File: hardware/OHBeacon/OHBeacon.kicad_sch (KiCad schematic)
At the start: 10 parts, among them J1 Conn_01x04_Socket, SW1 SW_Push, U1 ESP32-C3-WROOM-02

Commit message: new sch
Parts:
- added C1, C10, C11, C12, C13, C14, C2, C3, C4, C5, C6, C7, C8, C9: 0.1uF, Capacitor_SMD:C_0603_1608Metric, symbol Device:C
- added C18: 1.0uF, Capacitor_SMD:C_0603_1608Metric, symbol Device:C
- added C19, C20: 4.7uF, Capacitor_SMD:C_0603_1608Metric, symbol Device:C
- added D1, D10, D11, D12, D2, D3, D4, D5, D6, D7, D8, D9: WS2812B, LED_SMD:LED_WS2812B_PLCC4_5.0x5.0mm_P3.2mm, symbol LED:WS2812B
- added D14, D30: MDB6S, Package_SO:TSSOP-4_4.4x5mm_P4mm, symbol Diode_Bridge:MDB6S
- added J2, J3, J5, J6: Conn_01x01_Pin, Connector_Wire:SolderWire-2sqmm_1x01_D2mm_OD3.9mm, symbol Connector:Conn_01x01_Pin
- added J4: USB_C_Receptacle_PowerOnly_6P, Connector_USB:USB_C_Receptacle_GCT_USB4135-GF-A_6P_TopMnt_Horizontal, symbol Connector:USB_C_Receptacle_PowerOnly_6P
- added J7: Conn_01x02_Pin, Connector_PinSocket_2.54mm:PinSocket_1x02_P2.54mm_Vertical, symbol Connector:Conn_01x02_Pin
- added Q1: DMG2305UX-7, DMG2305UX-7:SOT91P240X110-3N_DMG2305UX-7, symbol DMG2305UX-7:DMG2305UX-7
- added R1, R5: 10k, Resistor_SMD:R_0603_1608Metric, symbol Device:R
- added R6, R7, R8: 100k, Resistor_SMD:R_0603_1608Metric, symbol Device:R
- added R9: 1k, Resistor_SMD:R_0603_1608Metric, symbol Device:R
- added SW2: SW_Push, Button_Switch_THT:SW_PUSH_6mm, symbol Switch:SW_Push
- added U2: BQ24074RGT, Package_DFN_QFN:VQFN-16-1EP_3x3mm_P0.5mm_EP1.6x1.6mm, symbol Battery_Management:BQ24074RGT
- added U3: AP2112K-3.3, Package_TO_SOT_SMD:SOT-23-5, symbol Regulator_Linear:AP2112K-3.3
- C17: value 0.1uF -> 4.7uF
- SW1: footprint Buttons_Switches_THT.pretty-master:SW_PUSH_6mm -> Button_Switch_THT:SW_PUSH_6mm
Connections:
- net +3.3V: now also C1.1, C10.1, C11.1, C12.1, C18.1, C2.1, C3.1, C4.1, C5.1, C6.1, C7.1, C8.1, C9.1, D1.1 (VDD), D10.1 (VDD), D11.1 (VDD), D12.1 (VDD), D2.1 (VDD), D3.1 (VDD), D4.1 (VDD), D5.1 (VDD), D6.1 (VDD), D7.1 (VDD), D8.1 (VDD), D9.1 (VDD), R1.1, U3.5 (VOUT)
- net GND: now also U1.19 (GND), U1.9 (GND), C1.2, C10.2, C11.2, C12.2, C13.2, C14.2, C18.2, C19.2, C2.2, C20.2, C3.2, C4.2, C5.2, C6.2, C7.2, C8.2, C9.2, D1.3 (VSS), D10.3 (VSS), D11.3 (VSS), D12.3 (VSS), D14.2 (-), D2.3 (VSS), D3.3 (VSS), D30.2 (-), D4.3 (VSS), D5.3 (VSS), D6.3 (VSS), D7.3 (VSS), D8.3 (VSS), D9.3 (VSS), J4.A12 (GND), J4.B12 (GND), J7.1 (Pin_1), R5.1, R7.1, R8.1, R9.1, SW2.1, U2.14 (TMR), U2.17 (VSS), U2.4 (~{CE}), U2.8 (VSS), U3.2 (GND)
- net EN: now reaches R3.2, SW1.2, U1.2 (EN)
- net EN: now also C13.1; no longer C17.1
- net DIN: now reaches U1.15 (IO3)
- net DIN: now also D1.4 (DIN)
- net IO9: now reaches U1.8 (IO9)
- net IO9: now also C14.1, R1.2, SW2.2
- new net: C20.1, U2.10 (OUT), U2.11 (OUT)
- new net: Q1.3, R8.2, U3.3 (EN)
- new net: R5.2, U2.1 (TS)
- new net: R9.2, U2.16 (ISET)
- new net: R7.2, U2.5 (EN2)
- new net: R6.2, U2.6 (EN1)
- new net: D30.3, J3.1 (Pin_1)
- new net: D30.4, J2.1 (Pin_1)
- new net: D10.2 (DOUT), D12.4 (DIN)
- new net: D5.2 (DOUT), D7.4 (DIN)
- new net: D3.2 (DOUT), D5.4 (DIN)
- new net: D1.2 (DOUT), D3.4 (DIN)
- new net: D4.2 (DOUT), D6.4 (DIN)
- new net: D2.2 (DOUT), D4.4 (DIN)
- new net: D11.4 (DIN), D9.2 (DOUT)
- new net: D7.2 (DOUT), D9.4 (DIN)
- new net: D10.4 (DIN), D8.2 (DOUT)
- new net: D6.2 (DOUT), D8.4 (DIN)
- new net: D14.3, J6.1 (Pin_1)
- new net: D14.4, J5.1 (Pin_1)
- new net +5V: C17.1, D14.1 (+), D30.1 (+), J4.A9 (VBUS), J4.B9 (VBUS), Q1.1, R6.1, U2.13 (IN)
- new net +BATT: C19.1, J7.2 (Pin_2), Q1.2, U2.2 (BAT), U2.3 (BAT), U3.1 (VIN)
- new net DCON: D11.2 (DOUT), D2.4 (DIN)
- no-connect marks 0 -> 18
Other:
- removed sheet LED_strip
- removed sheet power_input
- note added: "DRILL FOOTPRINT WITH 2MM DIAMETER WORKS FOR HAND SOLDER POGO PIN PART NUMBER: 0906-8-15-20-76-14-11-0"
- moved on the sheet: C15, C16, J1, R2, R4, U1

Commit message: prelim beacon pcb
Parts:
- added R10: 100k, Resistor_SMD:R_0603_1608Metric, symbol Device:R
- added R11: 0, Resistor_SMD:R_0603_1608Metric, symbol Device:R
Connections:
- net +5V: now also R10.2
- net GND: now also R10.1, R11.1
- net at U2.12 (ILIM): now also R11.2
- no-connect marks 18 -> 17
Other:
- moved on the sheet: R6, R7

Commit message: Changed some stuff in the schematic :)
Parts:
- added C21: 1.0uF, Capacitor_SMD:C_0603_1608Metric, symbol Device:C
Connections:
- net +BATT: now also C21.1
- net GND: now also C21.2
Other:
- moved on the sheet: C17

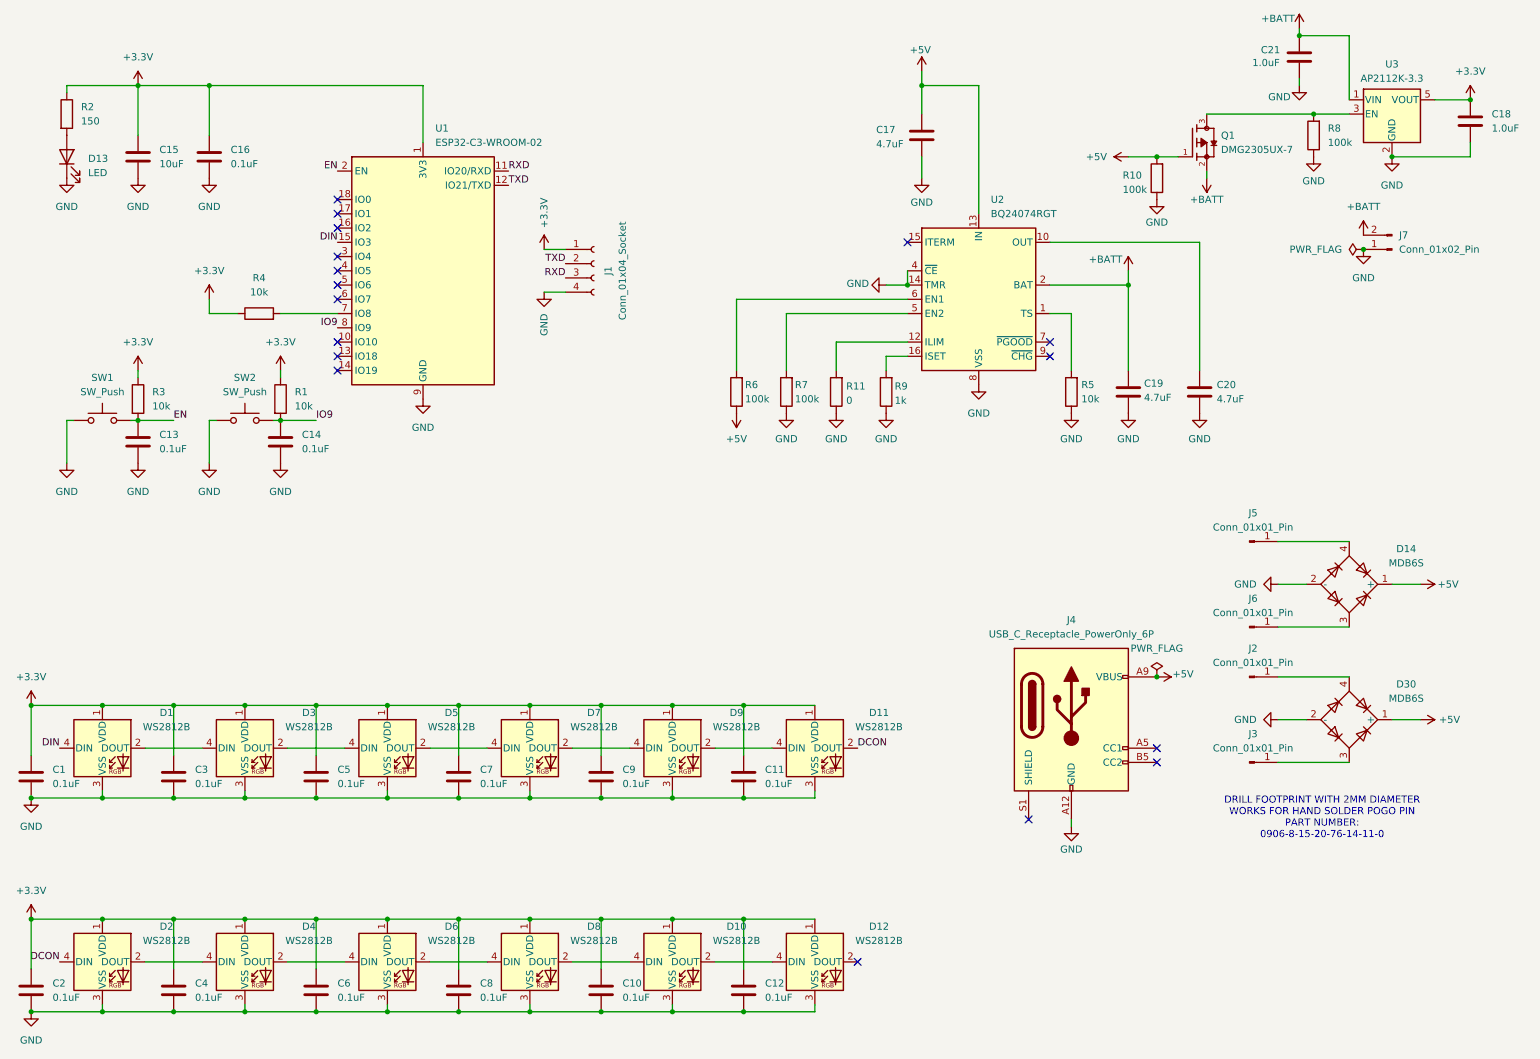
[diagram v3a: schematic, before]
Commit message: new oh beacon schematic and early routing
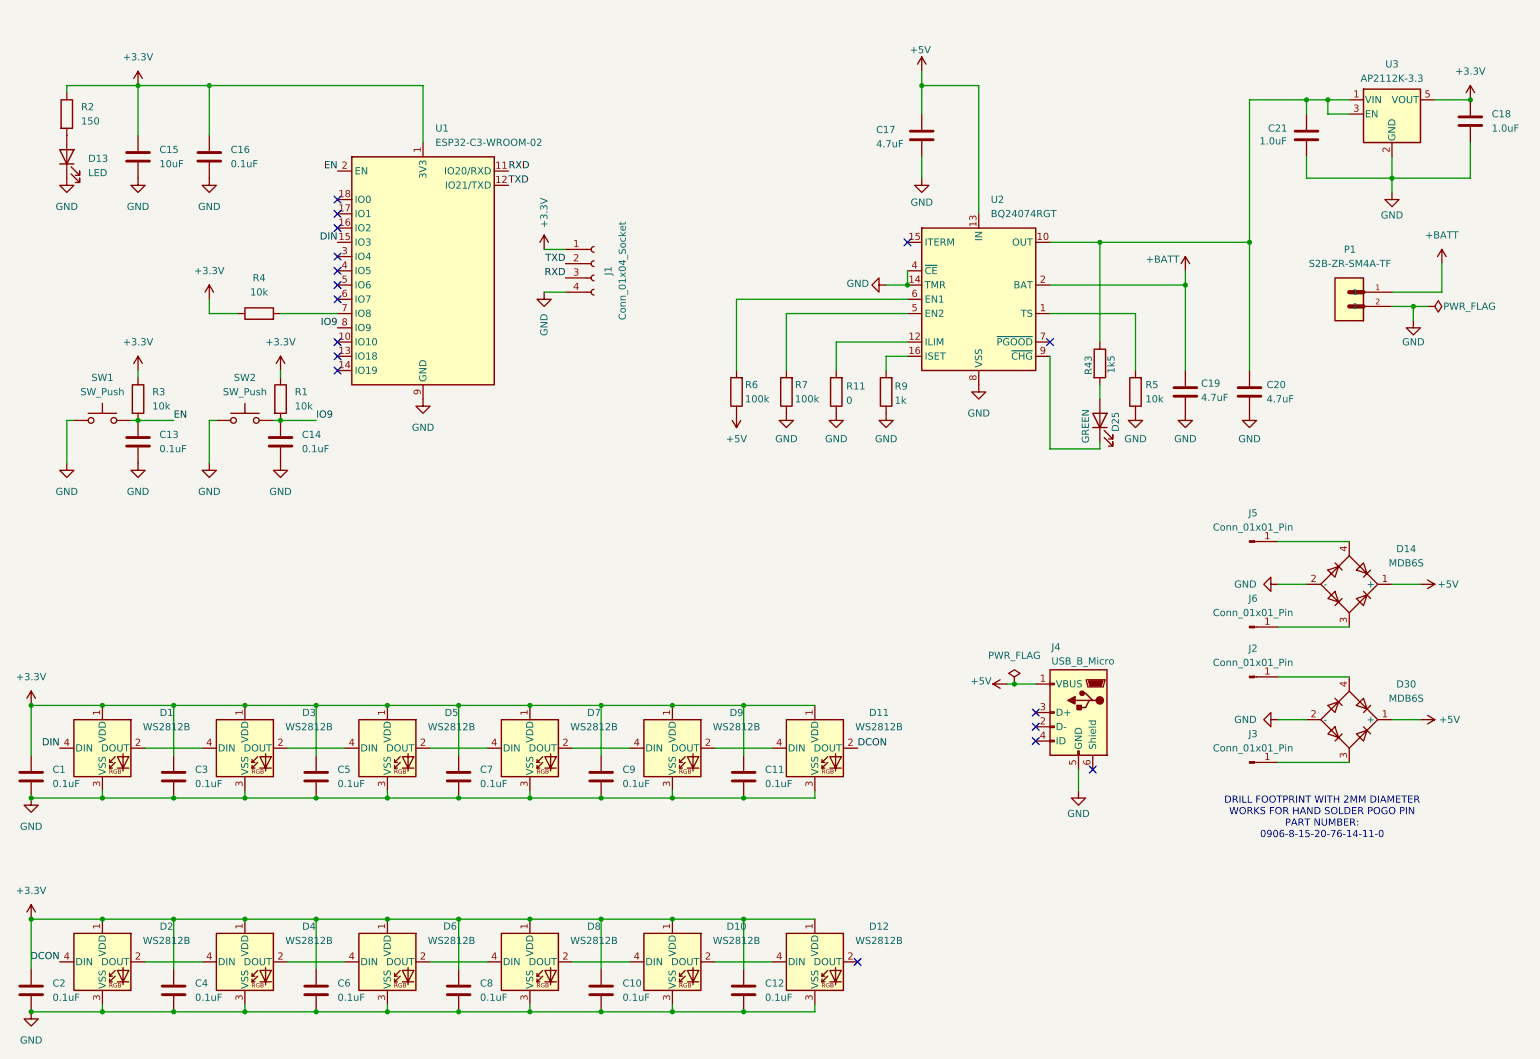
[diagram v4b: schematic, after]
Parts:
- removed J4: USB_C_Receptacle_PowerOnly_6P, Connector_USB:USB_C_Receptacle_GCT_USB4135-GF-A_6P_TopMnt_Horizontal, symbol Connector:USB_C_Receptacle_PowerOnly_6P
- removed J7: Conn_01x02_Pin, Connector_PinSocket_2.54mm:PinSocket_1x02_P2.54mm_Vertical, symbol Connector:Conn_01x02_Pin
- removed Q1: DMG2305UX-7, DMG2305UX-7:SOT91P240X110-3N_DMG2305UX-7, symbol DMG2305UX-7:DMG2305UX-7
- removed R10, R8: 100k, Resistor_SMD:R_0603_1608Metric, symbol Device:R
- added D25: GREEN, LED_SMD:LED_0603_1608Metric, symbol Device:LED
- added J4: USB_B_Micro, Connector_USB:USB_Micro-B_Wuerth_629105150521, symbol Connector:USB_B_Micro
- added P1: S2B-ZR-SM4A-TF, custom footprints:JST_S2B-ZR-SM4A-TF, symbol JST CONNECTOR:S2B-ZR-SM4A-TF
- added R43: 1k5, Resistor_SMD:R_0402_1005Metric, symbol Device:R
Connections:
- net +5V: now also J4.1 (VBUS)
- net +BATT: now also P1.1; no longer C21.1, U3.1 (VIN)
- net GND: now also J4.5 (GND), P1.2
- net at C20.1, U2.10 (OUT), U2.11 (OUT): now also C21.1, U3.1 (VIN), U3.3 (EN), R43.1
- net at U2.9 (~{CHG}): now also D25.1 (K)
- new net: D25.2 (A), R43.2
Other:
- moved on the sheet: C19, C20, C21, R5

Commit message: fml
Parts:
- removed C10, C11, C12, C9: 0.1uF, Capacitor_SMD:C_0603_1608Metric, symbol Device:C
- removed D10, D7, D8, D9: WS2812B, LED_SMD:LED_WS2812B_PLCC4_5.0x5.0mm_P3.2mm, symbol LED:WS2812B
- removed D14, D30: MDB6S, Package_SO:TSSOP-4_4.4x5mm_P4mm, symbol Diode_Bridge:MDB6S
- C1, C2, C3, C4, C5, C6, C7, C8: footprint Capacitor_SMD:C_0603_1608Metric -> Capacitor_SMD:C_0805_2012Metric_Pad1.18x1.45mm_HandSolder
- C10: renamed from C16; footprint Capacitor_SMD:C_0603_1608Metric -> Capacitor_SMD:C_0805_2012Metric_Pad1.18x1.45mm_HandSolder
- C11: renamed from C13; footprint Capacitor_SMD:C_0603_1608Metric -> Capacitor_SMD:C_0805_2012Metric_Pad1.18x1.45mm_HandSolder
- C12: renamed from C14; footprint Capacitor_SMD:C_0603_1608Metric -> Capacitor_SMD:C_0805_2012Metric_Pad1.18x1.45mm_HandSolder
- C13: renamed from C19; footprint Capacitor_SMD:C_0603_1608Metric -> Capacitor_SMD:C_0805_2012Metric_Pad1.18x1.45mm_HandSolder
- C14: renamed from C20; footprint Capacitor_SMD:C_0603_1608Metric -> Capacitor_SMD:C_0805_2012Metric_Pad1.18x1.45mm_HandSolder
- C15: renamed from C17; footprint Capacitor_SMD:C_0603_1608Metric -> Capacitor_SMD:C_0805_2012Metric_Pad1.18x1.45mm_HandSolder
- C16: renamed from C21; footprint Capacitor_SMD:C_0603_1608Metric -> Capacitor_SMD:C_0805_2012Metric_Pad1.18x1.45mm_HandSolder
- C17: renamed from C18; footprint Capacitor_SMD:C_0603_1608Metric -> Capacitor_SMD:C_0805_2012Metric_Pad1.18x1.45mm_HandSolder
- C9: renamed from C15; footprint Capacitor_SMD:C_0603_1608Metric -> Capacitor_SMD:C_0805_2012Metric_Pad1.18x1.45mm_HandSolder
- D10: renamed from D25; footprint LED_SMD:LED_0603_1608Metric -> LED_SMD:LED_0805_2012Metric_Pad1.15x1.40mm_HandSolder
- D9: renamed from D13; value LED -> RED; footprint LED_SMD:LED_0603_1608Metric -> LED_SMD:LED_0805_2012Metric_Pad1.15x1.40mm_HandSolder
- J1: renamed from J5; footprint Connector_Wire:SolderWire-2sqmm_1x01_D2mm_OD3.9mm -> Connector_Wire:SolderWire-1sqmm_1x01_D1.4mm_OD3.9mm
- J2: renamed from J6; footprint Connector_Wire:SolderWire-2sqmm_1x01_D2mm_OD3.9mm -> Connector_Wire:SolderWire-1sqmm_1x01_D1.4mm_OD3.9mm
- J3: renamed from J2; footprint Connector_Wire:SolderWire-2sqmm_1x01_D2mm_OD3.9mm -> Connector_Wire:SolderWire-1sqmm_1x01_D1.4mm_OD3.9mm
- J4: renamed from J3; footprint Connector_Wire:SolderWire-2sqmm_1x01_D2mm_OD3.9mm -> Connector_Wire:SolderWire-1sqmm_1x01_D1.4mm_OD3.9mm
- R1: renamed from R2; value 150 -> 1K; footprint Resistor_SMD:R_0603_1608Metric -> Resistor_SMD:R_0805_2012Metric_Pad1.20x1.40mm_HandSolder
- R10: renamed from R11; footprint Resistor_SMD:R_0603_1608Metric -> Resistor_SMD:R_0805_2012Metric_Pad1.20x1.40mm_HandSolder
- R2: renamed from R3; footprint Resistor_SMD:R_0603_1608Metric -> Resistor_SMD:R_0805_2012Metric_Pad1.20x1.40mm_HandSolder
- R3: renamed from R1; footprint Resistor_SMD:R_0603_1608Metric -> Resistor_SMD:R_0805_2012Metric_Pad1.20x1.40mm_HandSolder
- R4: footprint Resistor_SMD:R_0603_1608Metric -> Resistor_SMD:R_0805_2012Metric_Pad1.20x1.40mm_HandSolder
- R5: renamed from R6; footprint Resistor_SMD:R_0603_1608Metric -> Resistor_SMD:R_0805_2012Metric_Pad1.20x1.40mm_HandSolder
- R6: renamed from R7; footprint Resistor_SMD:R_0603_1608Metric -> Resistor_SMD:R_0805_2012Metric_Pad1.20x1.40mm_HandSolder
- R7: renamed from R9; footprint Resistor_SMD:R_0603_1608Metric -> Resistor_SMD:R_0805_2012Metric_Pad1.20x1.40mm_HandSolder
- R8: renamed from R43; value 1k5 -> 1k; footprint Resistor_SMD:R_0402_1005Metric -> Resistor_SMD:R_0805_2012Metric_Pad1.20x1.40mm_HandSolder
- R9: renamed from R5; footprint Resistor_SMD:R_0603_1608Metric -> Resistor_SMD:R_0805_2012Metric_Pad1.20x1.40mm_HandSolder
- SW1: value SW_Push -> EN
- SW2: value SW_Push -> I09
- renumbered D3 to D2, D5 to D3, D11 to D4, D2 to D5, D4 to D6, D6 to D7, D12 to D8, J4 to J5, J1 to J6
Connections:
- net +5V: now also J1.1 (Pin_1), J3.1 (Pin_1)
- net GND: now also J2.1 (Pin_1), J4.1 (Pin_1)
- net at D8.4 (DIN): now also D7.2 (DOUT)
- net at D3.2 (DOUT): now also D4.4 (DIN)
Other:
- note removed: "DRILL FOOTPRINT WITH 2MM DIAMETER WORKS FOR HAND SOLDER POGO PIN PART NUMBER: 0906-8-15-20-76-14-11-0"
- moved on the sheet: C16, C17, D10, D4, D8, J1, J2, J3, R8, U3

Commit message: new charging
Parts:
- removed C15: 4.7uF, Capacitor_SMD:C_0805_2012Metric_Pad1.18x1.45mm_HandSolder, symbol Device:C
- removed J5: USB_B_Micro, Connector_USB:USB_Micro-B_Wuerth_629105150521, symbol Connector:USB_B_Micro
- removed R10: 0, Resistor_SMD:R_0805_2012Metric_Pad1.20x1.40mm_HandSolder, symbol Device:R
- removed U2: BQ24074RGT, Package_DFN_QFN:VQFN-16-1EP_3x3mm_P0.5mm_EP1.6x1.6mm, symbol Battery_Management:BQ24074RGT
- added C17: 0.1uF, Capacitor_SMD:C_0805_2012Metric_Pad1.18x1.45mm_HandSolder, symbol Device:C
- added J5: USB_C_Receptacle_PowerOnly_6P, Connector_USB:USB_C_Receptacle_GCT_USB4135-GF-A_6P_TopMnt_Horizontal, symbol Connector:USB_C_Receptacle_PowerOnly_6P
- added Q1: DMG2305UX-7, DMG2305UX-7:SOT91P240X110-3N_DMG2305UX-7, symbol DMG2305UX-7:DMG2305UX-7
- added U4: MCP73831-2-OT, Package_TO_SOT_SMD:SOT-23-5, symbol Battery_Management:MCP73831-2-OT
- C13, C14: value 4.7uF -> 10uF
- D10: value GREEN -> RED
- R5, R6: value 100k -> 5k1
- R7: value 1k -> 10k
- renumbered C16 to C15, C17 to C16
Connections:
- net +3.3V: now also Q1.2; no longer C1.1, C2.1, C3.1, C4.1, C5.1, C6.1, C7.1, C8.1, D1.1 (VDD), D2.1 (VDD), D3.1 (VDD), D4.1 (VDD), D5.1 (VDD), D6.1 (VDD), D7.1 (VDD), D8.1 (VDD)
- net +5V: now also C13.1, D10.2 (A), J5.A9 (VBUS), J5.B9 (VBUS), U4.4 (V_{DD}); no longer R5.1
- net +BATT: now also C14.1, C15.1, U3.1 (VIN), U3.3 (EN), U4.3 (V_{BAT}); no longer C13.1
- net GND: now also R5.1, R9.2, C17.2, J5.A12 (GND), J5.B12 (GND), U4.2 (V_{SS}); no longer R9.1
- net at R7.2: now also U4.5 (PROG)
- net at R6.2: now also J5.A5 (CC1)
- net at R5.2: now also J5.B5 (CC2)
- net at D10.1 (K): now also R8.1
- net at R8.2: now also U4.1 (STAT); no longer D10.2 (A)
- net IO7: now reaches U1.6 (IO7)
- net IO7: now also R9.1, C17.1, Q1.1
- new net BATT_VCC: C1.1, C2.1, C3.1, C4.1, C5.1, C6.1, C7.1, C8.1, D1.1 (VDD), D2.1 (VDD), D3.1 (VDD), D4.1 (VDD), D5.1 (VDD), D6.1 (VDD), D7.1 (VDD), D8.1 (VDD), Q1.3
- no-connect marks 17 -> 11

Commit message: get james approval
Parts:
- D9: value RED -> GREEN
- R7: value 10k -> 1k
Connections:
- net +3.3V: no longer Q1.2
- net +BATT: now also Q1.2
- net BATT_VCC renamed LED_VCC
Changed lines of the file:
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@@
 	(wire
 		(pts
-			(xy 31.75 152.4) (xy 31.75 151.13)
-		)
-		(stroke
-			(width 0)
-			(type default)
-		)
-	)
-	(wire
-		(pts
 			(xy 69.85 135.89) (xy 69.85 144.78)
 		)
@@
 	(wire
 		(pts
-			(xy 123.19 101.6) (xy 123.19 104.14)
+			(xy 31.75 135.89) (xy 44.45 135.89)
 		)
 		(stroke
@@
 	(wire
 		(pts
-			(xy 31.75 135.89) (xy 44.45 135.89)
+			(xy 82.55 173.99) (xy 95.25 173.99)
 		)
 		(stroke
@@
 	(wire
 		(pts
-			(xy 82.55 173.99) (xy 95.25 173.99)
+			(xy 44.45 135.89) (xy 44.45 144.78)
 		)
 		(stroke
@@
 	(wire
 		(pts
-			(xy 44.45 135.89) (xy 44.45 144.78)
+			(xy 82.55 189.23) (xy 82.55 190.5)
 		)
 		(stroke
@@
 	(wire
 		(pts
-			(xy 82.55 189.23) (xy 82.55 190.5)
+			(xy 191.77 41.91) (xy 209.55 41.91)
 		)
 		(stroke
@@
 	(wire
 		(pts
-			(xy 191.77 41.91) (xy 209.55 41.91)
+			(xy 181.61 30.48) (xy 184.15 30.48)
 		)
 		(stroke
@@
 	(wire
 		(pts
-			(xy 181.61 30.48) (xy 184.15 30.48)
+			(xy 62.23 85.09) (xy 63.5 85.09)
 		)
 		(stroke
@@
 	(wire
 		(pts
-			(xy 62.23 85.09) (xy 63.5 85.09)
+			(xy 31.75 151.13) (xy 31.75 152.4)
 		)
 		(stroke
@@
 	(wire
 		(pts
+			(xy 123.19 104.14) (xy 123.19 101.6)
+		)
+		(stroke
+			(width 0)
+			(type default)
+		)
+	)
+	(wire
+		(pts
 			(xy 110.49 54.61) (xy 114.3 54.61)
 		)
@@
 		)
 	)
-	(label "BATT_VCC"
+	(label "LED_VCC"
 		(at 107.95 173.99 0)
 		(effects
@@
 		)
 	)
-	(label "BATT_VCC"
+	(label "LED_VCC"
 		(at 107.95 135.89 0)
 		(effects
@@
 		)
 	)
-	(label "BATT_VCC"
-		(at 123.19 101.6 0)
+	(label "LED_VCC"
+		(at 123.19 104.14 0)
 		(effects
 			(font
@@
 	)
 	(symbol
-		(lib_id "power:+3.3V")
-		(at 123.19 116.84 180)
-		(unit 1)
-		(exclude_from_sim no)
-		(in_bom yes)
-		(on_board yes)
-		(dnp no)
-		(fields_autoplaced yes)
-		(property "Reference" "#PWR029"
-			(at 123.19 113.03 0)
-			(effects
-				(font
-					(size 1.27 1.27)
-				)
-				(hide yes)
-			)
-		)
-		(property "Value" "+3.3V"
-			(at 123.19 121.92 0)
-			(effects
-				(font
-					(size 1.27 1.27)
-				)
-			)
-		)
-		(property "Footprint" ""
-			(at 123.19 116.84 0)
-			(effects
-				(font
-					(size 1.27 1.27)
-				)
-				(hide yes)
-			)
-		)
-		(property "Datasheet" ""
-			(at 123.19 116.84 0)
-			(effects
-				(font
-					(size 1.27 1.27)
-				)
-				(hide yes)
-			)
-		)
-		(property "Description" "Power symbol creates a global label with name \"+3.3V\""
-			(at 123.19 116.84 0)
-			(effects
-				(font
-					(size 1.27 1.27)
-				)
-				(hide yes)
-			)
-		)
-		(pin "1"
-		)
-		(instances
-			(project "OHBeacon"
-				(path "/4e0e7048-b221-4c06-a0a7-7b0ffd7a96a3"
-					(reference "#PWR029")
-					(unit 1)
-				)
-			)
-		)
-	)
-	(symbol
 		(lib_id "Device:C")
 		(at 44.45 186.69 0)
@@
 			)
 		)
-		(property "Value" "RED"
+		(property "Value" "GREEN"
 			(at 29.21 40.9574 90)
 			(effects
@@
 	)
 	(symbol
+		(lib_id "power:+BATT")
+		(at 123.19 116.84 180)
+		(unit 1)
+		(exclude_from_sim no)
+		(in_bom yes)
+		(on_board yes)
+		(dnp no)
+		(property "Reference" "#PWR030"
+			(at 123.19 113.03 0)
+			(effects
+				(font
+					(size 1.27 1.27)
+				)
+				(hide yes)
+			)
+		)
+		(property "Value" "+BATT"
+			(at 123.19 120.904 0)
+			(effects
+				(font
+					(size 1.27 1.27)
+				)
+			)
+		)
+		(property "Footprint" ""
+			(at 123.19 116.84 0)
+			(effects
+				(font
+					(size 1.27 1.27)
+				)
+				(hide yes)
+			)
+		)
+		(property "Datasheet" ""
+			(at 123.19 116.84 0)
+			(effects
+				(font
+					(size 1.27 1.27)
+				)
+				(hide yes)
+			)
+		)
+		(property "Description" "Power symbol creates a global label with name \"+BATT\""
+			(at 123.19 116.84 0)
+			(effects
+				(font
+					(size 1.27 1.27)
+				)
+				(hide yes)
+			)
+		)
+		(pin "1"
+		)
+		(instances
+			(project "OHBeacon"
+				(path "/4e0e7048-b221-4c06-a0a7-7b0ffd7a96a3"
+					(reference "#PWR030")
+					(unit 1)
+				)
+			)
+		)
+	)
+	(symbol
 		(lib_id "power:PWR_FLAG")
 		(at 195.58 149.86 270)
@@
 	)
 	(symbol
+		(lib_id "power:PWR_FLAG")
+		(at 123.19 101.6 0)
+		(unit 1)
+		(exclude_from_sim no)
+		(in_bom yes)
+		(on_board yes)
+		(dnp no)
+		(fields_autoplaced yes)
+		(property "Reference" "#FLG03"
+			(at 123.19 99.695 0)
+			(effects
+				(font
+					(size 1.27 1.27)
+				)
+				(hide yes)
+			)
+		)
+		(property "Value" "PWR_FLAG"
+			(at 125.73 100.3299 0)
+			(effects
+				(font
+					(size 1.27 1.27)
+				)
+				(justify left)
+			)
+		)
+		(property "Footprint" ""
+			(at 123.19 101.6 0)
+			(effects
+				(font
+					(size 1.27 1.27)
+				)
+				(hide yes)
+			)
+		)
+		(property "Datasheet" "~"
+			(at 123.19 101.6 0)
+			(effects
+				(font
+					(size 1.27 1.27)
+				)
+				(hide yes)
+			)
+		)
+		(property "Description" "Special symbol for telling ERC where power comes from"
+			(at 123.19 101.6 0)
+			(effects
+				(font
+					(size 1.27 1.27)
+				)
+				(hide yes)
+			)
+		)
+		(pin "1"
+		)
+		(instances
+			(project "OHBeacon"
+				(path "/4e0e7048-b221-4c06-a0a7-7b0ffd7a96a3"
+					(reference "#FLG03")
+					(unit 1)
+				)
+			)
+		)
+	)
+	(symbol
 		(lib_id "Switch:SW_Push")
 		(at 57.15 85.09 0)
@@
 			)
 		)
-		(property "Value" "10k"
+		(property "Value" "1k"
 			(at 163.83 48.768 0)
 			(effects
